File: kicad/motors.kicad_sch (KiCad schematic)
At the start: 27 parts, among them J10 Conn_01x04_Pin, J11 Conn_01x04_Pin, J12 Conn_01x04_Pin, J5 Conn_02x03_Odd_Even, J6 Conn_01x04_Pin, J7 Conn_02x03_Odd_Even, J8 Conn_01x04_Pin, J9 Conn_02x03_Odd_Even, U3 TMC2209-LA

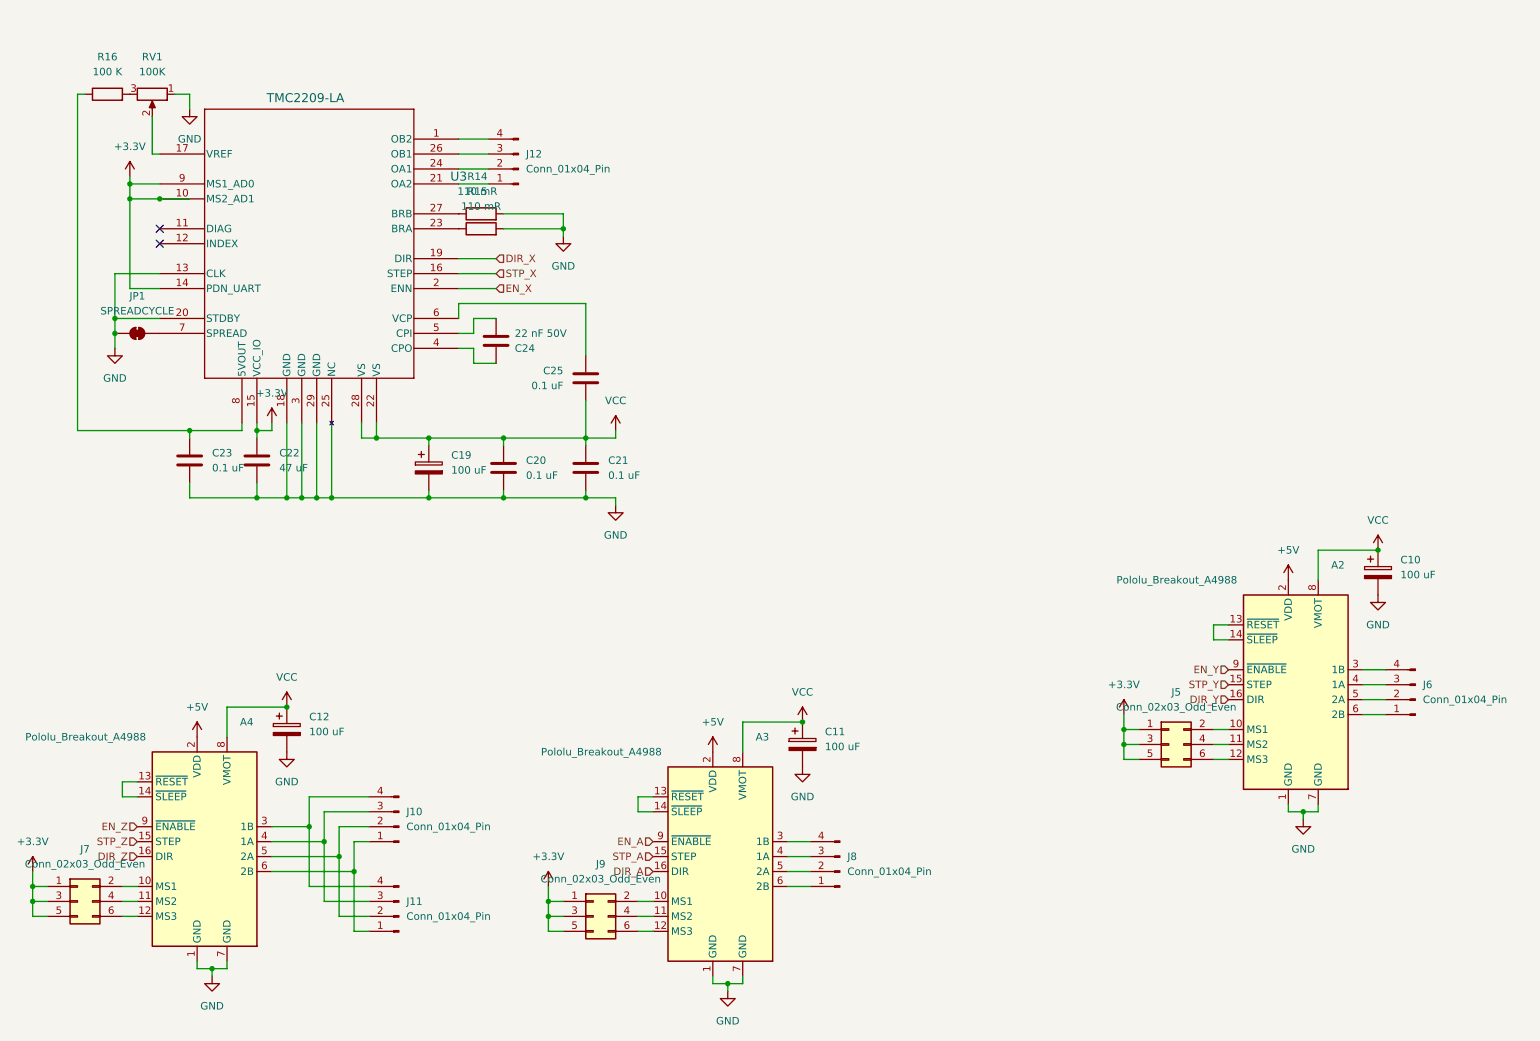
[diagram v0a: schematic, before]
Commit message: Miniaturizing the stepper drivers. They're still too big
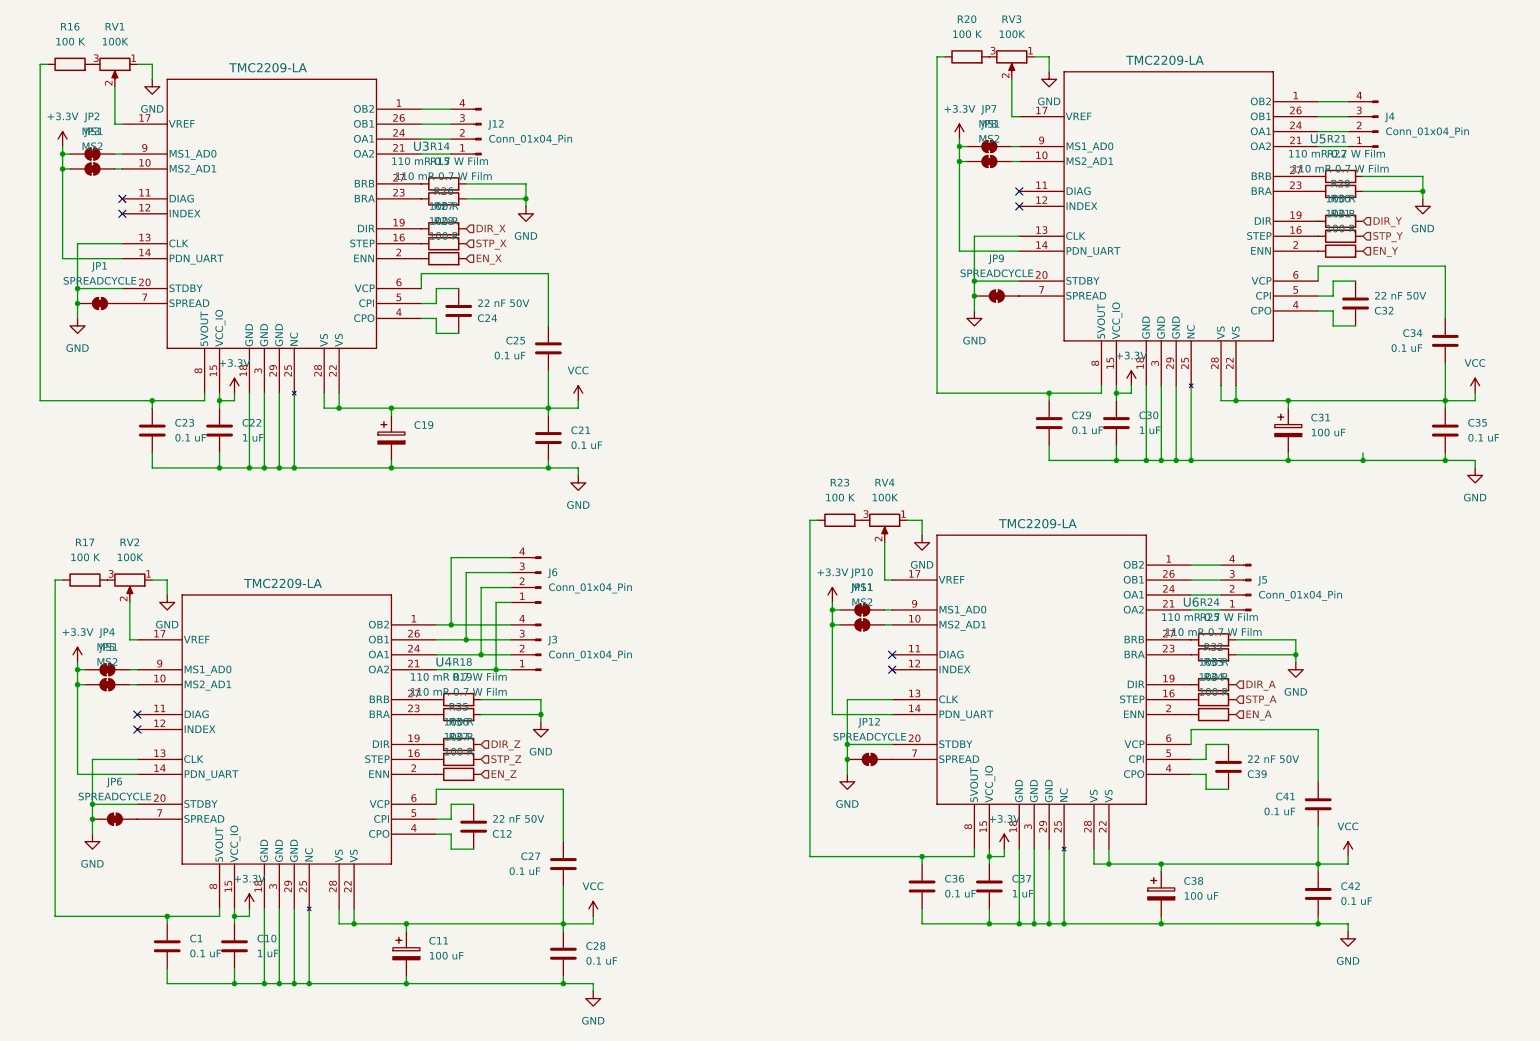
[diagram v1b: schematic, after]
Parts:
- removed A2, A3, A4: Pololu_Breakout_A4988, Module:Pololu_Breakout-16_15.2x20.3mm, symbol Driver_Motor:Pololu_Breakout_A4988
- removed C10, C12: 100 uF, Capacitor_THT:C_Disc_D3.0mm_W1.6mm_P2.50mm, symbol Device:C_Polarized
- removed C20: 0.1 uF, Capacitor_SMD:C_0603_1608Metric, symbol Device:C
- removed J10, J11, J8: Conn_01x04_Pin, Connector_JST:JST_XH_B4B-XH-A_1x04_P2.50mm_Vertical, symbol Connector:Conn_01x04_Pin
- removed J5, J7, J9: Conn_02x03_Odd_Even, Connector_PinHeader_2.54mm:PinHeader_2x03_P2.54mm_Vertical, symbol Connector_Generic:Conn_02x03_Odd_Even
- added C1, C27, C28, C29, C34, C35, C36, C41, C42: 0.1 uF, Capacitor_SMD:C_0402_1005Metric, symbol Device:C
- added C10, C30, C37: 1 uF, Capacitor_SMD:C_0402_1005Metric, symbol Device:C
- added C12, C32, C39: 22 nF 50V, Capacitor_SMD:C_0402_1005Metric, symbol Device:C
- added C31, C38: 100 uF, Capacitor_THT:C_Radial_D6.3mm_H11.0mm_P2.50mm, symbol Device:C_Polarized
- added J3, J4, J5: Conn_01x04_Pin, Connector_JST:JST_XH_B4B-XH-A_1x04_P2.50mm_Vertical, symbol Connector:Conn_01x04_Pin
- added JP10, JP2, JP4, JP7: MS1, Jumper:SolderJumper-2_P1.3mm_Bridged_RoundedPad1.0x1.5mm, symbol Jumper:SolderJumper_2_Bridged
- added JP11, JP3, JP5, JP8: MS2, Jumper:SolderJumper-2_P1.3mm_Bridged_RoundedPad1.0x1.5mm, symbol Jumper:SolderJumper_2_Bridged
- added JP12, JP6, JP9: SPREADCYCLE, Jumper:SolderJumper-2_P1.3mm_Bridged_RoundedPad1.0x1.5mm, symbol Jumper:SolderJumper_2_Bridged
- added R17, R20, R23: 100 K, Resistor_SMD:R_0402_1005Metric, symbol Device:R
- added R18, R19, R21, R22, R24, R25: 110 mR 0.7 W Film, Resistor_SMD:R_2010_5025Metric, symbol Device:R
- added R26, R27, R28, R29, R30, R31, R32, R33, R34, R35, R36, R37: 100 R, Resistor_SMD:R_0402_1005Metric, symbol Device:R
- added RV2, RV3, RV4: 100K, Potentiometer_SMD:Potentiometer_Bourns_TC33X_Vertical, symbol Device:R_Potentiometer
- added U4, U5, U6: TMC2209-LA, rephat-parts:QFN28_5X5_TRI-M, symbol rephat-symbols:TMC2209-LA
- C11, C19: footprint Capacitor_THT:C_Disc_D3.0mm_W1.6mm_P2.50mm -> Capacitor_THT:C_Radial_D6.3mm_H11.0mm_P2.50mm
- C21, C23, C24, C25: footprint Capacitor_SMD:C_0603_1608Metric -> Capacitor_SMD:C_0402_1005Metric
- C22: value 47 uF -> 1 uF; footprint Capacitor_SMD:C_1206_3216Metric -> Capacitor_SMD:C_0402_1005Metric
- R14, R15: value 110 mR -> 110 mR 0.7 W Film; footprint Resistor_SMD:R_0603_1608Metric -> Resistor_SMD:R_2010_5025Metric
- R16: footprint Resistor_SMD:R_0603_1608Metric -> Resistor_SMD:R_0402_1005Metric
- RV1: footprint (none) -> Potentiometer_SMD:Potentiometer_Bourns_TC33X_Vertical
- U3: footprint QFN28_5X5_TRI -> rephat-parts:QFN28_5X5_TRI-M
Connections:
- net +3.3V: now also C10.1, C30.1, C37.1, JP10.1 (A), JP11.1 (A), JP2.1 (A), JP3.1 (A), JP4.1 (A), JP5.1 (A), JP7.1 (A), JP8.1 (A), U4.14 (PDN_UART), U4.15 (VCC_IO), U5.14 (PDN_UART), U5.15 (VCC_IO), U6.14 (PDN_UART), U6.15 (VCC_IO); no longer U3.10 (MS2_AD1), U3.9 (MS1_AD0)
- net DIR_A: now also R32.2
- net DIR_X: now also R26.2; no longer U3.19 (DIR)
- net DIR_Y: now also R29.2
- net DIR_Z: now also R35.2
- net EN_A: now also R34.2
- net EN_X: now also R28.2; no longer U3.2 (ENN)
- net EN_Y: now also R31.2
- net EN_Z: now also R37.2
- net GND: now also C1.2, C10.2, C28.2, C29.2, C30.2, C31.2, C35.2, C36.2, C37.2, C38.2, C42.2, JP12.1 (A), JP6.1 (A), JP9.1 (A), R18.2, R19.2, R21.2, R22.2, R24.2, R25.2, RV2.1, RV3.1, RV4.1, U4.13 (CLK), U4.18 (GND), U4.20 (STDBY), U4.25 (NC), U4.29 (GND), U4.3 (GND), U5.13 (CLK), U5.18 (GND), U5.20 (STDBY), U5.25 (NC), U5.29 (GND), U5.3 (GND), U6.13 (CLK), U6.18 (GND), U6.20 (STDBY), U6.25 (NC), U6.29 (GND), U6.3 (GND)
- net STP_A: now also R33.2
- net STP_X: now also R27.2; no longer U3.16 (STEP)
- net STP_Y: now also R30.2
- net STP_Z: now also R36.2
- net VCC: now also C27.1, C28.1, C31.1, C34.1, C35.1, C38.1, C41.1, C42.1, U4.22 (VS), U4.28 (VS), U5.22 (VS), U5.28 (VS), U6.22 (VS), U6.28 (VS)
- net at J6.1 (Pin_1): now also J3.1 (Pin_1), U4.21 (OA2)
- net at J6.2 (Pin_2): now also J3.2 (Pin_2), U4.24 (OA1)
- net at J6.3 (Pin_3): now also J3.3 (Pin_3), U4.26 (OB1)
- net at J6.4 (Pin_4): now also J3.4 (Pin_4), U4.1 (OB2)
- new net: R29.1, U5.19 (DIR)
- new net: JP12.2 (B), U6.7 (SPREAD)
- new net: C1.1, R17.1, U4.8 (5VOUT)
- new net: R17.2, RV2.3
- new net: R35.1, U4.19 (DIR)
- new net: R25.1, U6.23 (BRA)
- new net: JP7.2 (B), U5.9 (MS1_AD0)
- new net: RV3.2, U5.17 (VREF)
- new net: R20.2, RV3.3
- new net: R19.1, U4.23 (BRA)
- new net: R33.1, U6.16 (STEP)
- new net: JP6.2 (B), U4.7 (SPREAD)
- new net: C32.1, U5.5 (CPI)
- new net: C32.2, U5.4 (CPO)
- new net: JP10.2 (B), U6.9 (MS1_AD0)
- new net: C29.1, R20.1, U5.8 (5VOUT)
- new net: J5.4 (Pin_4), U6.1 (OB2)
- new net: JP11.2 (B), U6.10 (MS2_AD1)
- new net: RV4.2, U6.17 (VREF)
- new net: R32.1, U6.19 (DIR)
- new net: R34.1, U6.2 (ENN)
- new net: J5.1 (Pin_1), U6.21 (OA2)
- new net: J5.2 (Pin_2), U6.24 (OA1)
- new net: J5.3 (Pin_3), U6.26 (OB1)
- new net: R24.1, U6.27 (BRB)
- new net: C39.2, U6.4 (CPO)
- new net: C39.1, U6.5 (CPI)
- new net: C41.2, U6.6 (VCP)
- new net: C36.1, R23.1, U6.8 (5VOUT)
- new net: JP3.2 (B), U3.10 (MS2_AD1)
- new net: R27.1, U3.16 (STEP)
- new net: R26.1, U3.19 (DIR)
- new net: R28.1, U3.2 (ENN)
- new net: JP2.2 (B), U3.9 (MS1_AD0)
- new net: JP5.2 (B), U4.10 (MS2_AD1)
- new net: R36.1, U4.16 (STEP)
- new net: RV2.2, U4.17 (VREF)
- new net: R37.1, U4.2 (ENN)
- new net: R18.1, U4.27 (BRB)
- new net: C12.2, U4.4 (CPO)
- new net: C12.1, U4.5 (CPI)
- new net: C27.2, U4.6 (VCP)
- new net: JP4.2 (B), U4.9 (MS1_AD0)
- new net: R22.1, U5.23 (BRA)
- new net: R31.1, U5.2 (ENN)
- new net: JP8.2 (B), U5.10 (MS2_AD1)
- new net: J4.1 (Pin_1), U5.21 (OA2)
- new net: J4.2 (Pin_2), U5.24 (OA1)
- new net: J4.3 (Pin_3), U5.26 (OB1)
- new net: J4.4 (Pin_4), U5.1 (OB2)
- new net: R21.1, U5.27 (BRB)
- new net: R23.2, RV4.3
- new net: C34.2, U5.6 (VCP)
- new net: JP9.2 (B), U5.7 (SPREAD)
- new net: R30.1, U5.16 (STEP)
- no-connect marks 2 -> 8
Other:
- moved on the sheet: C19, C21, C22, C23, C24, C25, J12, JP1, R14, R15, R16, RV1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

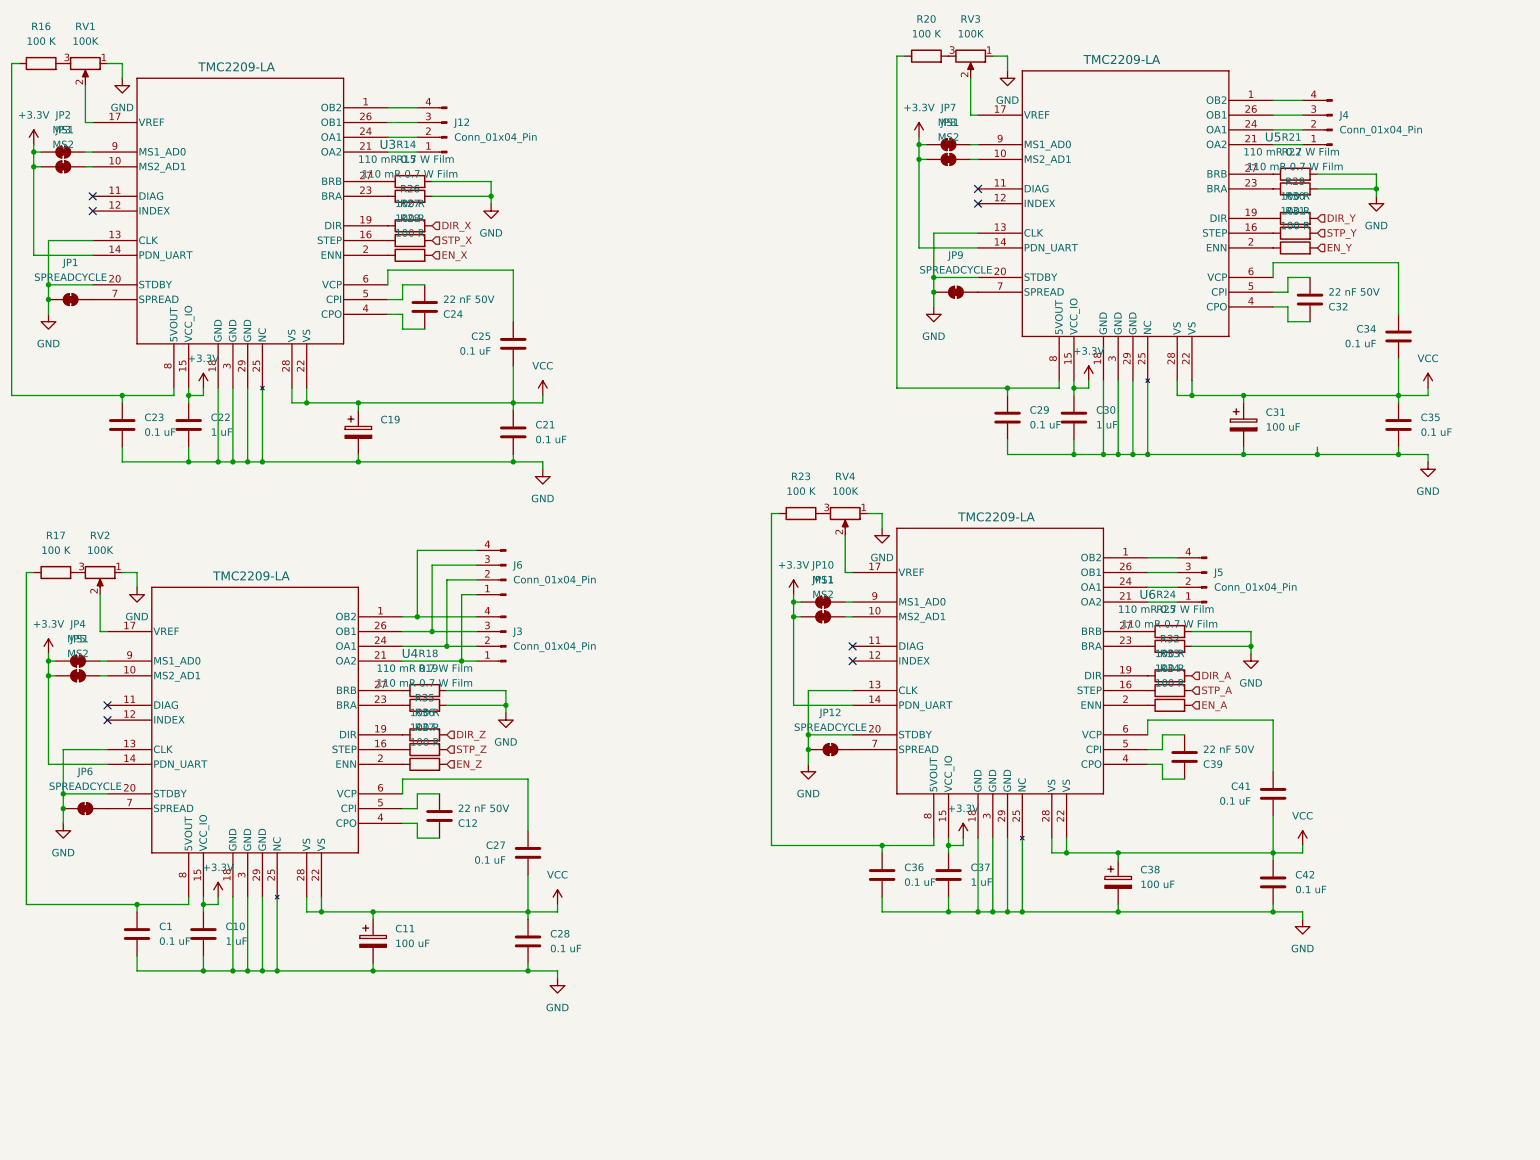
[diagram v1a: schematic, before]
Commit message: TMC2209->TMC2100, endstop protection optimization
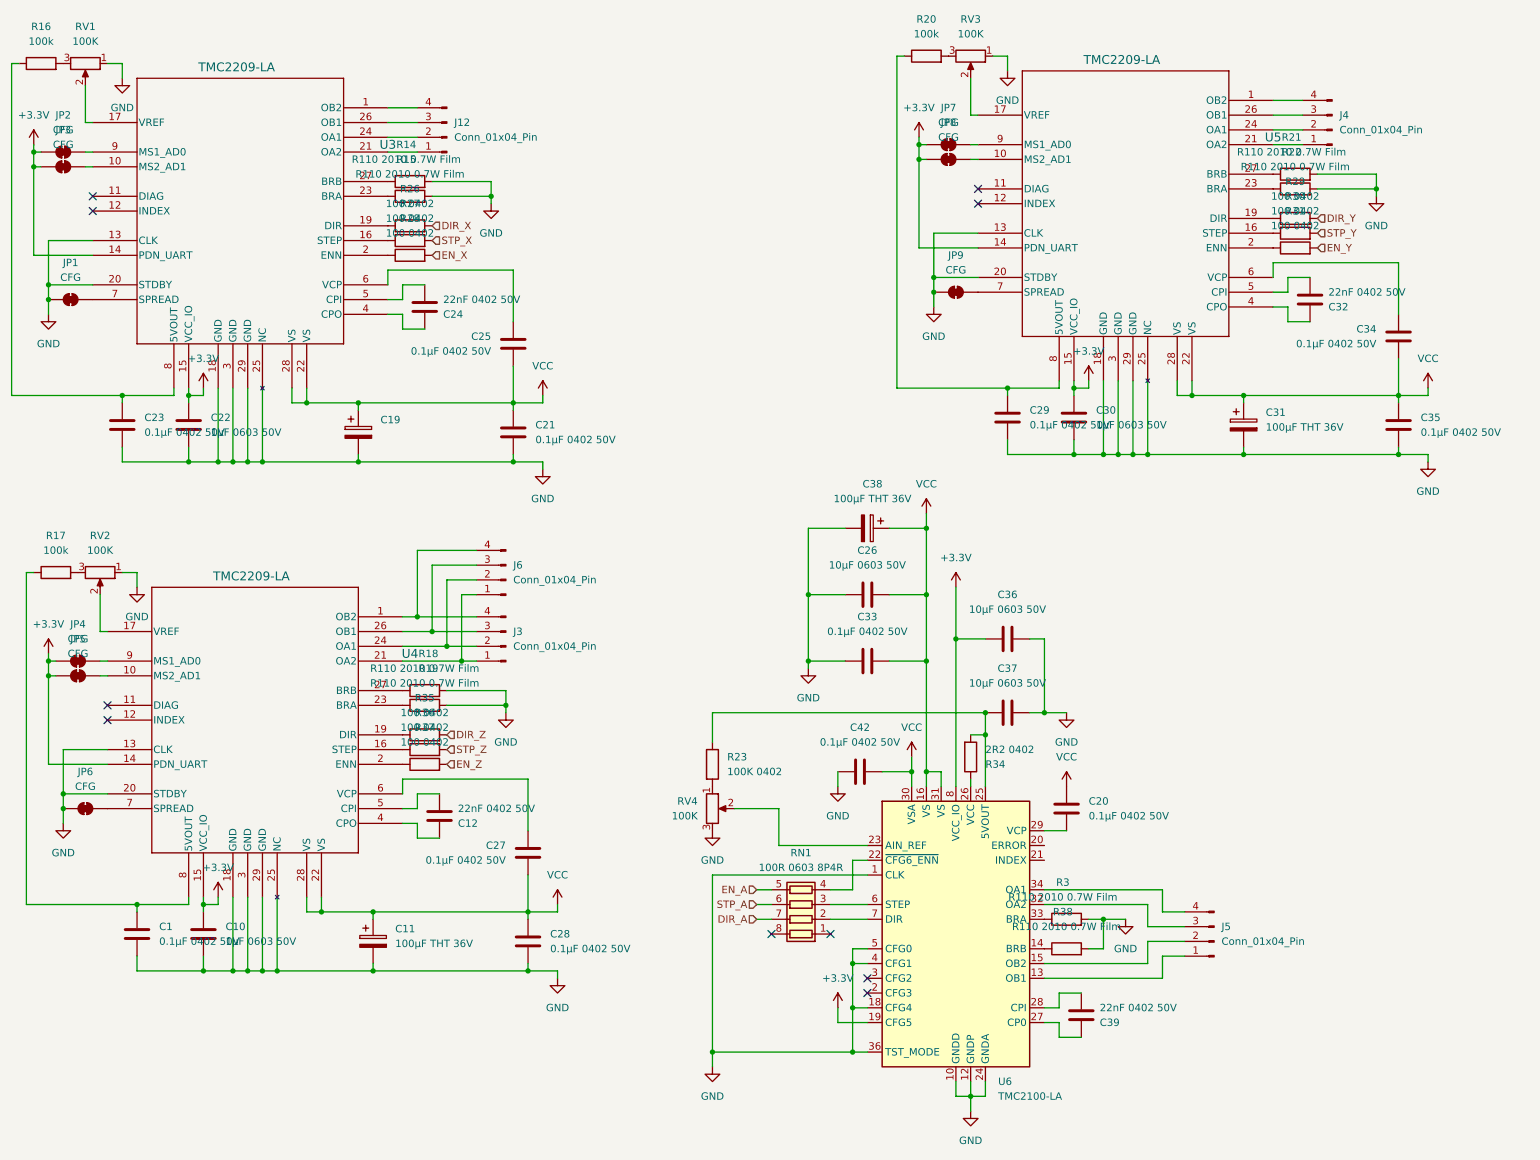
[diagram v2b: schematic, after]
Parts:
- removed C41: 0.1 uF, Capacitor_SMD:C_0402_1005Metric, symbol Device:C
- removed JP10: MS1, Jumper:SolderJumper-2_P1.3mm_Bridged_RoundedPad1.0x1.5mm, symbol Jumper:SolderJumper_2_Bridged
- removed JP11: MS2, Jumper:SolderJumper-2_P1.3mm_Bridged_RoundedPad1.0x1.5mm, symbol Jumper:SolderJumper_2_Bridged
- removed JP12: SPREADCYCLE, Jumper:SolderJumper-2_P1.3mm_Bridged_RoundedPad1.0x1.5mm, symbol Jumper:SolderJumper_2_Bridged
- removed R24, R25: 110 mR 0.7 W Film, Resistor_SMD:R_2010_5025Metric, symbol Device:R
- removed R32, R33: 100 R, Resistor_SMD:R_0402_1005Metric, symbol Device:R
- removed U6: TMC2209-LA, rephat-parts:QFN28_5X5_TRI-M, symbol rephat-symbols:TMC2209-LA
- added C20, C33: 0.1μF 0402 50V, Capacitor_SMD:C_0402_1005Metric, symbol Device:C
- added C26: 10μF 0603 50V, Capacitor_SMD:C_0402_1005Metric, symbol Device:C
- added R3, R38: R110 2010 0.7W Film, Resistor_SMD:R_2010_5025Metric, symbol Device:R
- added RN1: 100R 0603 8P4R, Resistor_SMD:R_Array_Concave_4x0603, symbol Device:R_Pack04
- added U6: TMC2100-LA, Package_DFN_QFN:QFN-36-1EP_5x6mm_P0.5mm_EP3.6x4.1mm_ThermalVias, symbol Driver_Motor:TMC2100-LA
- C1, C21, C23, C25, C27, C28, C29, C34, C35, C42: value 0.1 uF -> 0.1μF 0402 50V
- C10, C22, C30: value 1 uF -> 1μF 0603 50V
- C11, C19, C31, C38: value 100 uF -> 100μF THT 36V
- C12, C24, C32, C39: value 22 nF 50V -> 22nF 0402 50V
- C36: value 0.1 uF -> 10μF 0603 50V
- C37: value 1 uF -> 10μF 0603 50V
- JP1, JP6, JP9: value SPREADCYCLE -> CFG
- JP2, JP4, JP7: value MS1 -> CFG
- JP3, JP5, JP8: value MS2 -> CFG
- R14, R15, R18, R19, R21, R22: value 110 mR 0.7 W Film -> R110 2010 0.7W Film
- R16, R17, R20: value 100 K -> 100k
- R23: value 100 K -> 100K 0402
- R26, R27, R28, R29, R30, R31, R35, R36, R37: value 100 R -> 100 0402
- R34: value 100 R -> 2R2 0402
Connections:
- net +3.3V: now also C36.1, U6.19 (CFG5), U6.8 (VCC_IO); no longer C37.1
- net DIR_A: now also RN1.7 (R2.2)
- net EN_A: now also RN1.5 (R4.2); no longer R34.2
- net GND: now also C42.1, RV4.3, C26.1, C33.1, R3.2, R38.2, U6.1 (CLK), U6.10 (GNDD), U6.11 (GNDD), U6.12 (GNDP), U6.18 (CFG4), U6.24 (GNDA), U6.35 (GNDP), U6.36 (TST_MODE), U6.37 (GNDD), U6.4 (CFG1), U6.5 (CFG0); no longer C42.2, RV4.1
- net STP_A: now also RN1.6 (R3.2)
- net VCC: now also C42.2, C20.2, C26.2, C33.2, U6.16 (VS), U6.30 (VSA), U6.31 (VS); no longer C42.1
- net at J5.4 (Pin_4): now also U6.34 (OA1)
- net at RV4.2: now also U6.23 (AIN_REF)
- net at R34.1: now also U6.26 (VCC)
- net at J5.1 (Pin_1): now also U6.13 (OB1)
- net at J5.2 (Pin_2): now also U6.15 (OB2)
- net at J5.3 (Pin_3): now also U6.32 (OA2)
- net at C39.2: now also U6.27 (CP0)
- net at C39.1: now also U6.28 (CPI)
- net at R23.1: now also C37.1, R34.2, U6.25 (5VOUT); no longer C36.1
- net at R23.2: now also RV4.1; no longer RV4.3
- new net: R3.1, U6.33 (BRA)
- new net: RN1.2 (R2.1), U6.7 (DIR)
- new net: RN1.3 (R3.1), U6.6 (STEP)
- new net: RN1.4 (R4.1), U6.22 (~{CFG6_ENN})
- new net: C20.1, U6.29 (VCP)
- new net: R38.1, U6.14 (BRB)
- no-connect marks 8 -> 10
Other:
- moved on the sheet: C38, C39, C42, J5, R23, RV4
